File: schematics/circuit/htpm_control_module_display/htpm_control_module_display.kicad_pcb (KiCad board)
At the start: 2 copper layers, 73.7 x 48.3 mm, 58 parts, among them J1 Conn_01x10_Socket, J2 Conn_01x10_Socket

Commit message: Updated text location and specified product number placement.
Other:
- board text added: "JLCJLCJLCJLC"
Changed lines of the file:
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@@
   (gr_rect (start 111.76 73.66) (end 185.42 121.92)
     (stroke (width 0.1) (type default)) (fill none) (layer "Edge.Cuts"))
-  (gr_text "HTP!m CONTROL Module Display" (at 114.3 114.3 180) (layer "B.SilkS")
+  (gr_text "HTP!m CONTROL Module Display" (at 149.86 111.76) (layer "B.SilkS")
     (effects (font (size 1.5 1.5) (thickness 0.3) bold) (justify left bottom mirror))
   )
+  (gr_text "JLCJLCJLCJLC" (at 139.7 114.3) (layer "B.SilkS")
+    (effects (font (size 1 1) (thickness 0.15)) (justify left bottom mirror))
+  )
   (segment (start 154.94 106.68) (end 152.4 104.14) (width 0.25) (layer "F.Cu") (net 1))

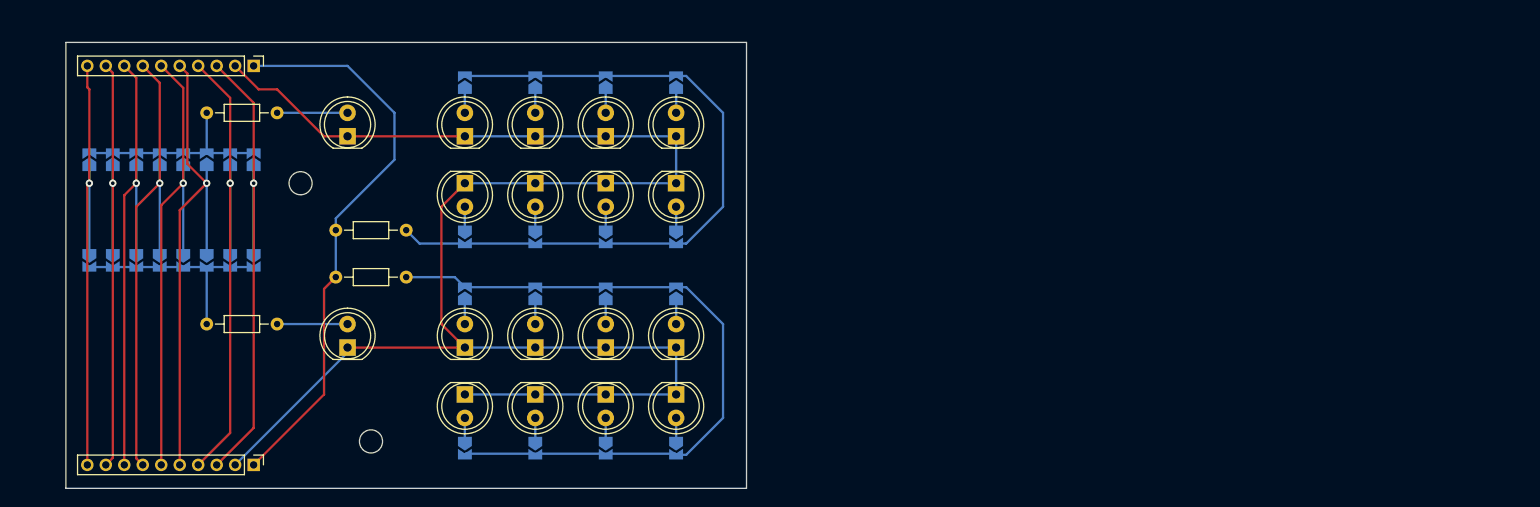
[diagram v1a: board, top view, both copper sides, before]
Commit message: Condensed HTPm CONTROL Module Display PCB.
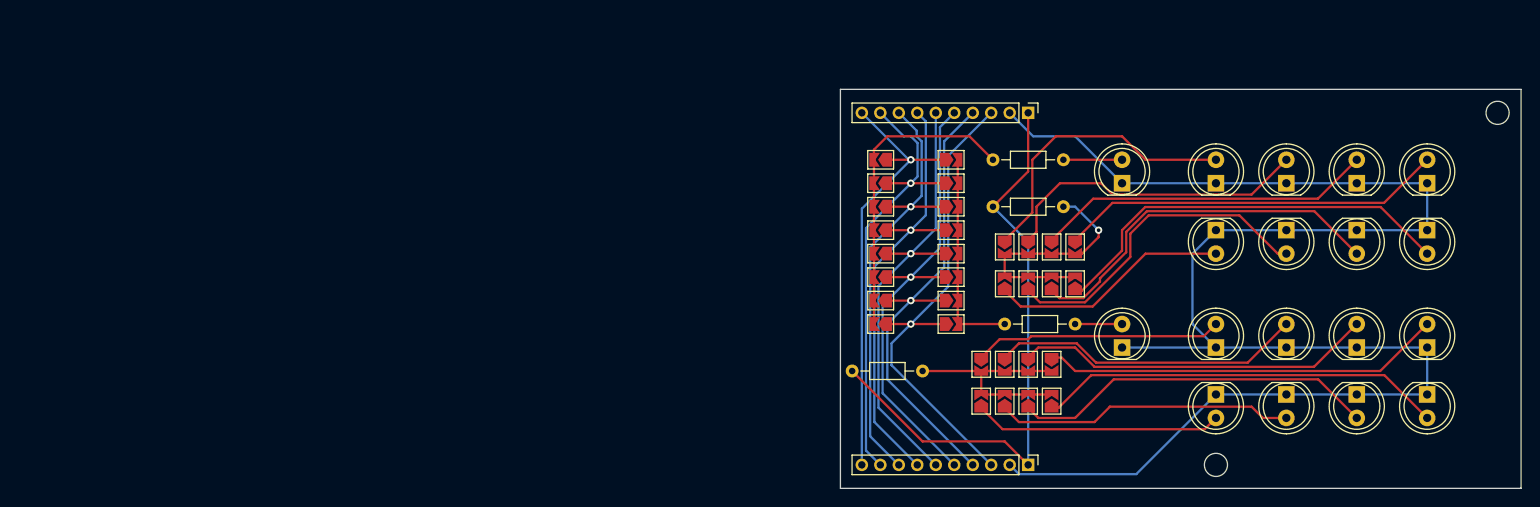
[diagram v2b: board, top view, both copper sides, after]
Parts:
- JP1, JP10, JP11, JP12, JP13, JP14, JP15, JP16, JP17, JP18, JP19, JP2, JP20, JP21, JP22, JP23, JP24, JP25, JP26, JP27, JP28, JP29, JP3, JP30, JP31, JP32, JP4, JP5, JP6, JP7, JP8, JP9: moved to F.Cu
- moved H1 129.8 mm to (266.7, 81.3)
- moved J1 94.3 mm to (215.9, 119.4)
- moved JP17 93.9 mm to (207.6, 86.4), turned to 0 degrees
- moved J2 92.1 mm to (215.9, 81.3)
- moved H2 91.5 mm to (236.2, 119.4)
- moved JP18 91.1 mm to (207.6, 88.9), turned to 0 degrees
- moved JP19 88.4 mm to (207.6, 91.4), turned to 0 degrees
- moved R2 86.4 mm to (213.4, 104.1)
- moved JP20 85.7 mm to (207.6, 94.0), turned to 0 degrees
- moved JP32 85.6 mm to (199.9, 86.4), turned to 180 degrees
- moved R1 85.2 mm to (212.1, 86.4)
- moved D1 84.0 mm to (226.1, 88.9)
- moved D2 83.8 mm to (226.1, 106.7)
- moved JP31 83.1 mm to (199.9, 88.9), turned to 180 degrees
- moved JP21 83.1 mm to (207.6, 96.5), turned to 0 degrees
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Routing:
- net Net-(JP10-B): track 76.3 -> 24.1 mm
- net Net-(JP1-B): track 76.3 -> 26.7 mm, vias 0 -> 1
- net Net-(D10-A): track 2.54 -> 45.2 mm
- net Net-(D18-A): track 2.54 -> 44.0 mm
- net Net-(D14-A): track 2.54 -> 43.3 mm
- net Net-(D6-A): track 2.54 -> 41.7 mm
- net Net-(D9-A): track 2.54 -> 40.6 mm
- net Net-(D17-A): track 2.54 -> 39.5 mm
- net Net-(D13-A): track 2.54 -> 38.8 mm
- net Net-(D5-A): track 2.54 -> 36.6 mm
- net Net-(D8-A): track 2.54 -> 35.6 mm
- net Net-(D4-A): track 2.54 -> 34.2 mm
- net Net-(D12-A): track 2.54 -> 33.7 mm
- net Net-(D16-A): track 2.54 -> 32.3 mm
- net Net-(D3-A): track 2.54 -> 31.9 mm
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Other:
- board size 73.7 x 48.3 mm -> 73.7 x 43.2 mm

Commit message: Repositioned HTPm CONTROL Module Display PCB.
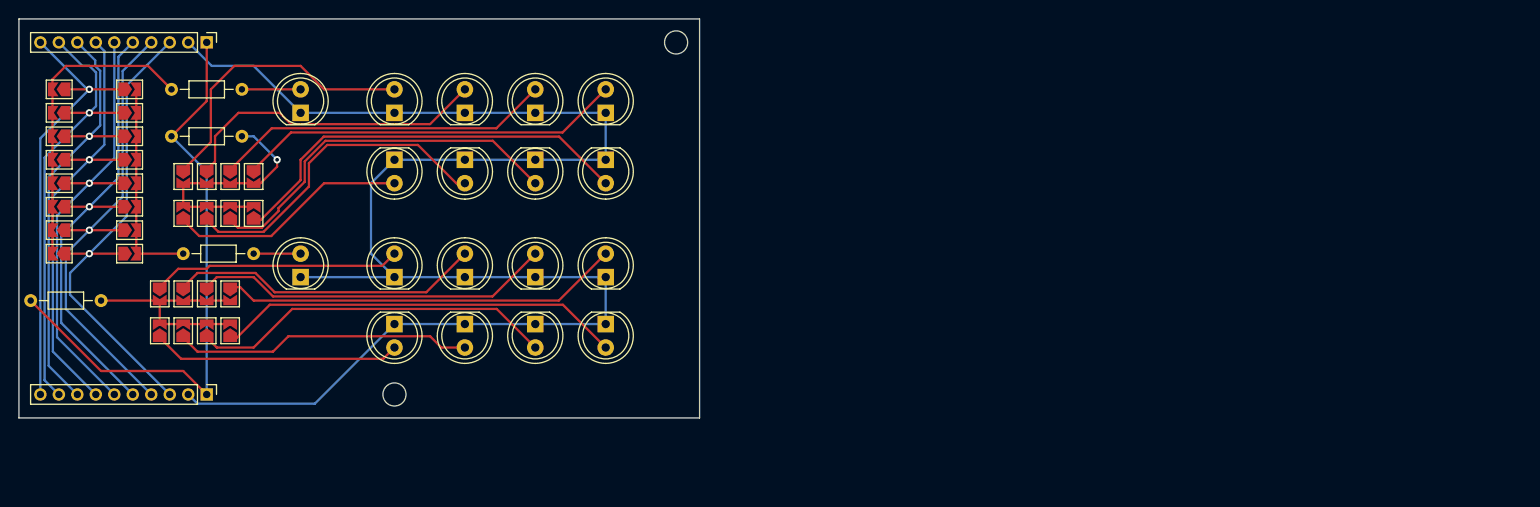
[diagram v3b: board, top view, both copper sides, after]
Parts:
- moved JP1 89.2 mm to (124.5, 88.2)
- moved JP10 89.2 mm to (124.5, 100.9)
- moved JP14 89.2 mm to (124.5, 104.9)
- moved JP5 89.2 mm to (124.5, 92.2)
- moved R2 89.2 mm to (124.5, 96.5)
- moved D1 89.2 mm to (137.2, 81.3)
- moved D11 89.2 mm to (147.3, 99.1)
- moved D12 89.2 mm to (154.9, 99.1)
- moved D13 89.2 mm to (162.6, 99.1)
- moved D15 89.2 mm to (147.3, 104.1)
- moved D16 89.2 mm to (154.9, 104.1)
- moved D17 89.2 mm to (162.6, 104.1)
- moved D2 89.2 mm to (137.2, 99.1)
- moved D3 89.2 mm to (147.3, 81.3)
- moved D4 89.2 mm to (154.9, 81.3)
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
